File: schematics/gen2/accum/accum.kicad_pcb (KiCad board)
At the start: 2 copper layers, 100 x 101.6 mm, 14 parts, among them U1 74LS574, U2 74LS138, U3 74LS02, U4 74LS245, U5 74LS245, U6 74LS245

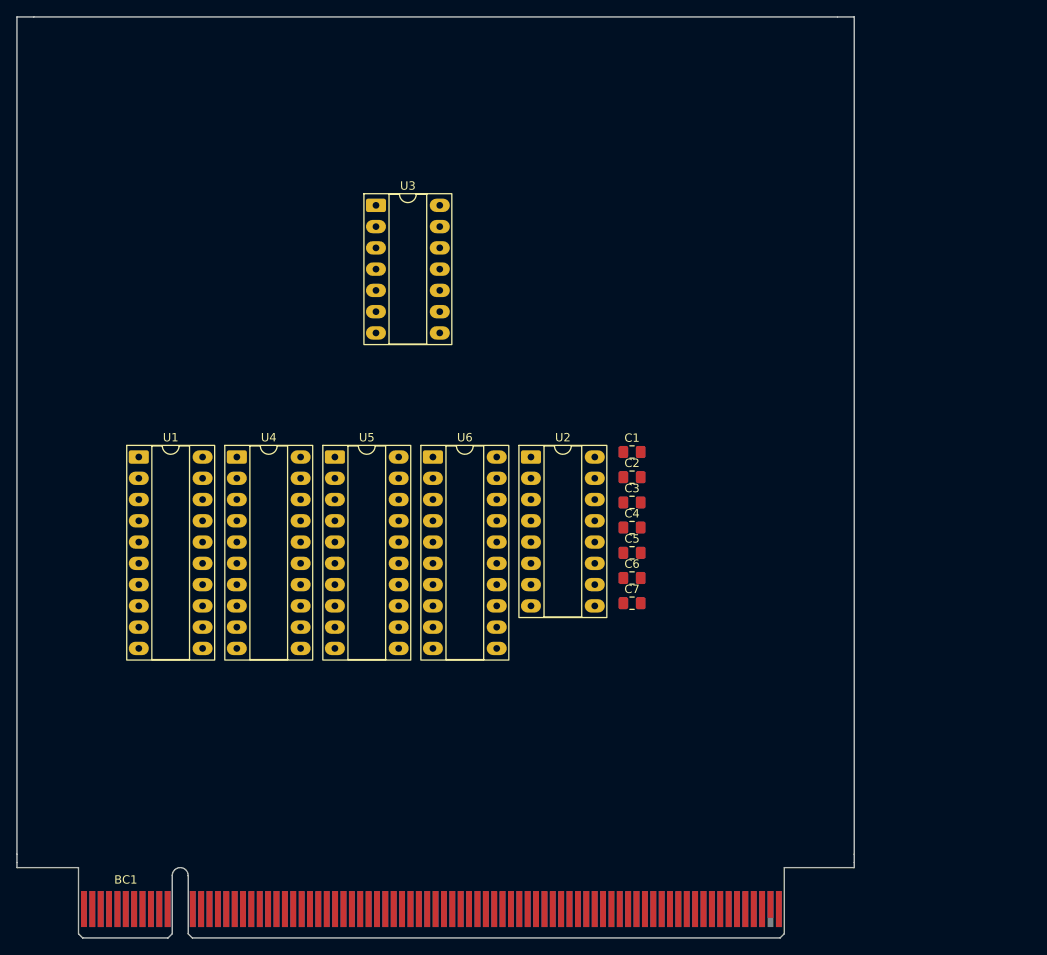
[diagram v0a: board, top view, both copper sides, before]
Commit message: fix: update accumulator schematic and routing rules
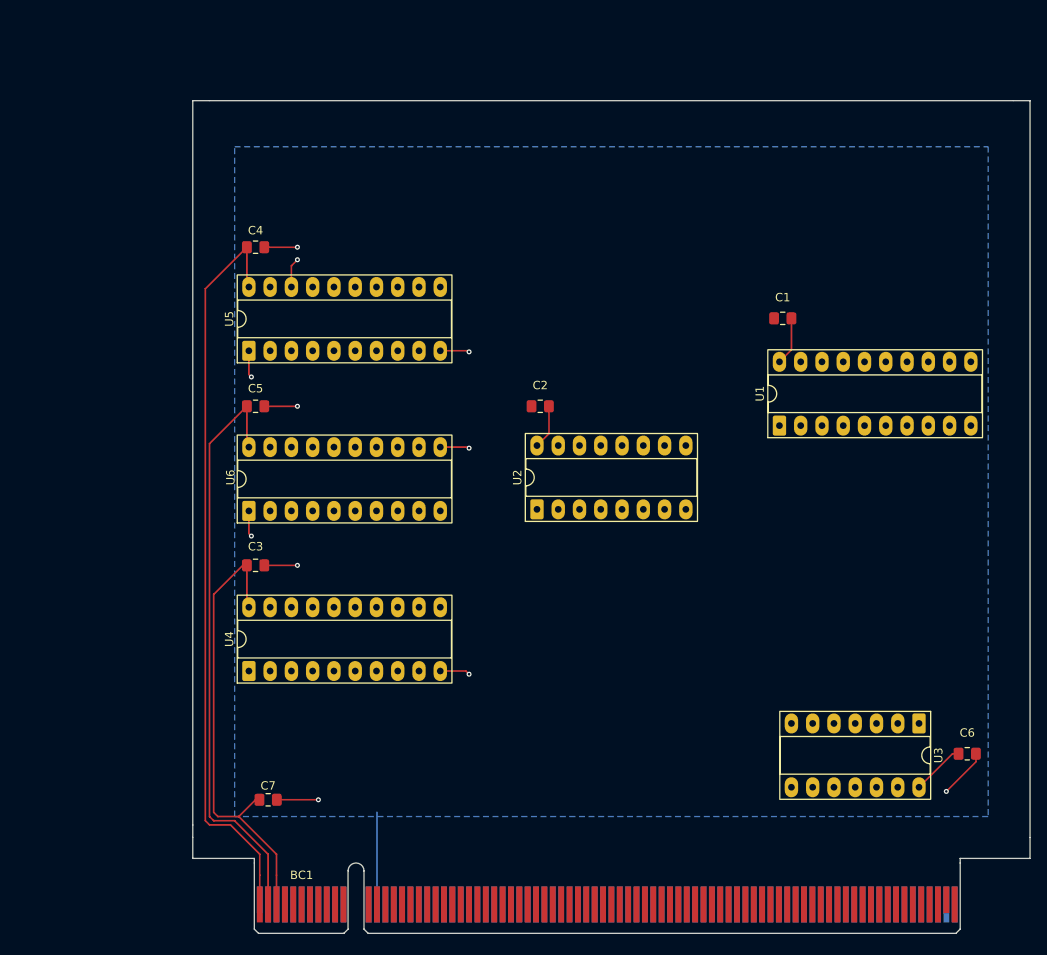
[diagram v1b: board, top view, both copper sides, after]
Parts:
- moved U3 89.6 mm to (186.7, 123.9), turned to -90 degrees
- moved U1 76.6 mm to (170.1, 88.3), turned to 90 degrees
- moved C4 56.1 mm to (107.5, 67.0)
- moved C7 49.4 mm to (109.0, 133.0)
- moved C5 48.2 mm to (107.5, 86.0)
- moved C3 45.6 mm to (107.5, 105.0)
- moved C6 45.2 mm to (192.5, 127.5)
- moved U4 25.6 mm to (106.7, 117.6), turned to 90 degrees
- moved C1 24.1 mm to (170.5, 75.5), turned to 180 degrees
- moved U6 22.9 mm to (106.7, 98.5), turned to 90 degrees
- moved BC1 21.0 mm to (108.0, 145.5)
- moved U5 16.3 mm to (106.7, 79.4), turned to 90 degrees
- moved C2 13.9 mm to (141.5, 86.0), turned to 180 degrees
- moved U2 6.29 mm to (141.1, 98.3), turned to 90 degrees
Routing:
- net VCC: track 0.00 -> 234.6 mm
- net GND: track 0.00 -> 54.3 mm, vias 0 -> 11
- added copper zone on B.Cu, net GND
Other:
- board size 100 x 101.6 mm -> 100 x 91.1 mm

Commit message: feat: accumulator pcb plate, with routes and gnd plate
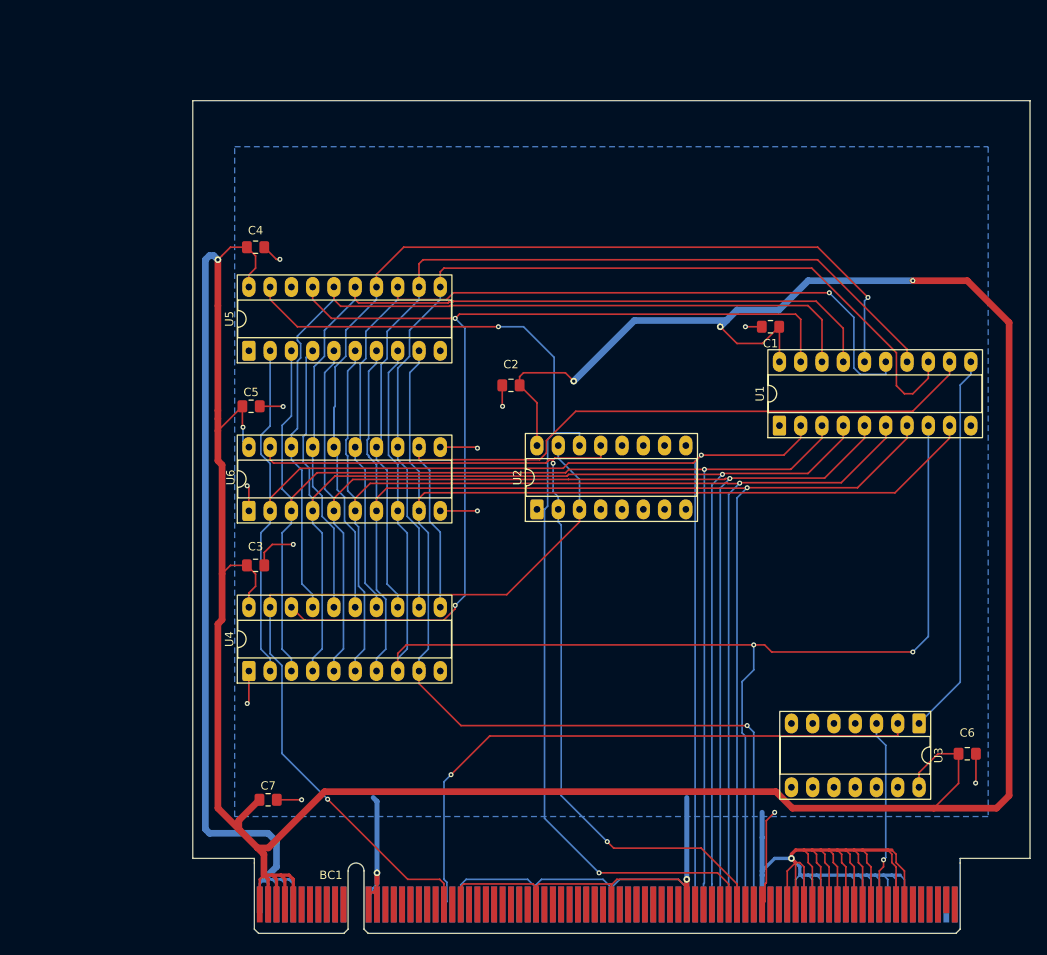
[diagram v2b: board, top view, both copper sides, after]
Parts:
- moved C2 4.30 mm to (138.0, 83.5)
- moved C1 1.77 mm to (169.0, 76.5)
- moved C5 0.54 mm to (107.0, 86.0)
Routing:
- net GND: track 54.3 -> 329.5 mm, vias 11 -> 15
- net VCC: track 234.6 -> 488.6 mm, vias 0 -> 5
- net /DATA7: track 0.00 -> 173.9 mm, vias 0 -> 1
- net /DATA6: track 0.00 -> 164.0 mm, vias 0 -> 2
- net /DATA0: track 0.00 -> 163.4 mm, vias 0 -> 1
- net /DATA1: track 0.00 -> 161.4 mm, vias 0 -> 1
- net /DATA2: track 0.00 -> 161.4 mm, vias 0 -> 1
- net /DATA3: track 0.00 -> 160.8 mm, vias 0 -> 1
- net /DATA4: track 0.00 -> 160.4 mm, vias 0 -> 1
- net /DATA5: track 0.00 -> 159.7 mm, vias 0 -> 1
- net /ACSHLEFT: track 0.00 -> 126.9 mm, vias 0 -> 2
- net /ACCUM0: track 0.00 -> 122.7 mm, vias 0 -> 2
- net /ACCUM3: track 0.00 -> 118.0 mm, vias 0 -> 1
- net /ACCUM6: track 0.00 -> 112.9 mm
- net /ACSHRIGHT: track 0.00 -> 111.5 mm, vias 0 -> 2
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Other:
- outline, holes or cut-outs redrawn

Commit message: fix: changed footprints in accum, added resistor and capacitor footrpint
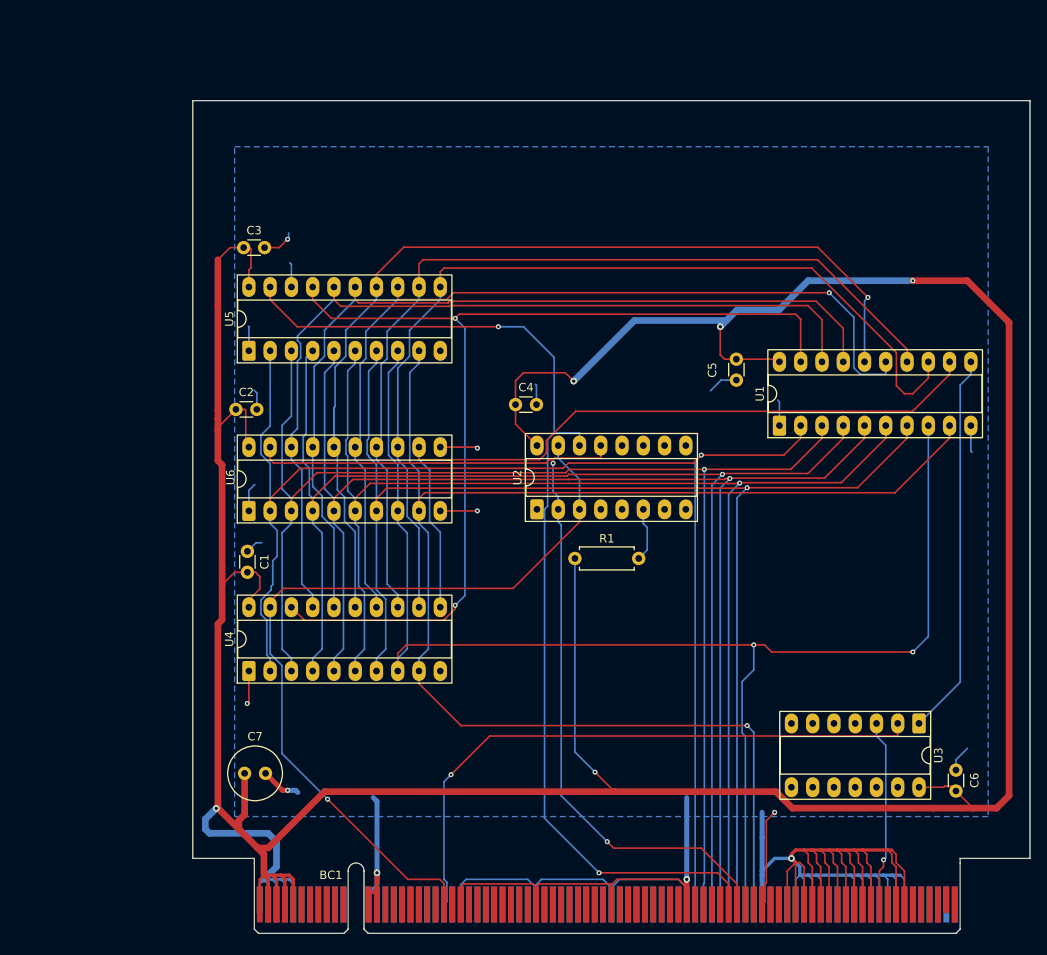
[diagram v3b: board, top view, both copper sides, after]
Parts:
- added R1: R, Resistor_THT:R_Axial_DIN0207_L6.3mm_D2.5mm_P7.62mm_Horizontal, F.Cu at (145.6, 104.2)
- C1, C2, C3, C4, C5, C6: footprint Capacitor_SMD:C_0805_2012Metric_Pad1.18x1.45mm_HandSolder -> Capacitor_THT:C_Disc_D3.0mm_W1.6mm_P2.50mm
- C7: footprint Capacitor_SMD:C_0805_2012Metric_Pad1.18x1.45mm_HandSolder -> Capacitor_THT:C_Radial_D6.3mm_H5.0mm_P2.50mm
- moved C1 69.0 mm to (106.5, 105.8), turned to 90 degrees
- moved C5 58.2 mm to (164.9, 80.4), turned to -90 degrees
- moved C3 38.0 mm to (106.1, 67.0)
- moved C4 36.3 mm to (138.6, 85.8)
- moved C2 33.0 mm to (105.2, 86.4), turned to 0 degrees
- moved C6 4.65 mm to (191.2, 131.9), turned to 90 degrees
- moved C7 4.23 mm to (106.2, 129.8)
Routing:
- net VCC: track 488.6 -> 444.7 mm
- net GND: track 329.5 -> 342.1 mm, vias 15 -> 9
- net Net-(U2-E3): track 0.00 -> 6.48 mm
- net /DATA0: track 163.4 -> 164.1 mm

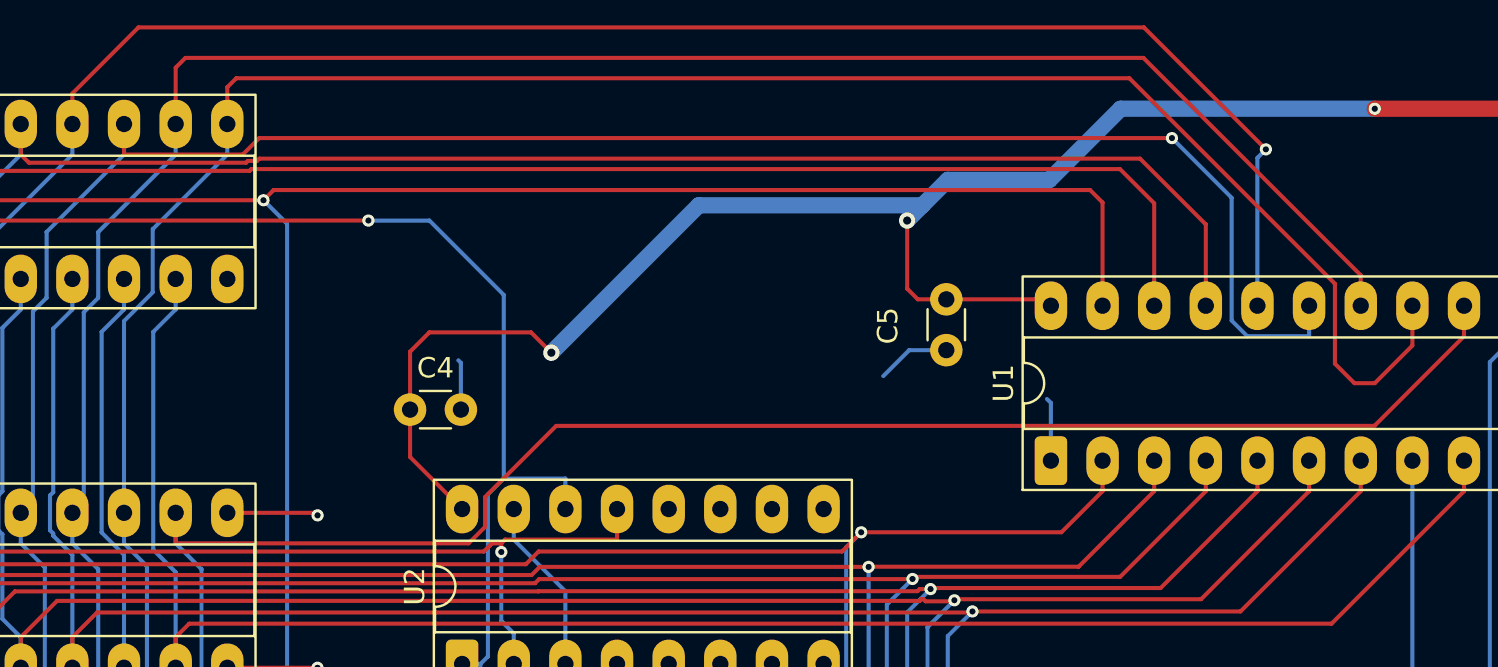
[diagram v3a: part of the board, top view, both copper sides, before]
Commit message: fix(accum): update segment connections and adjust routing
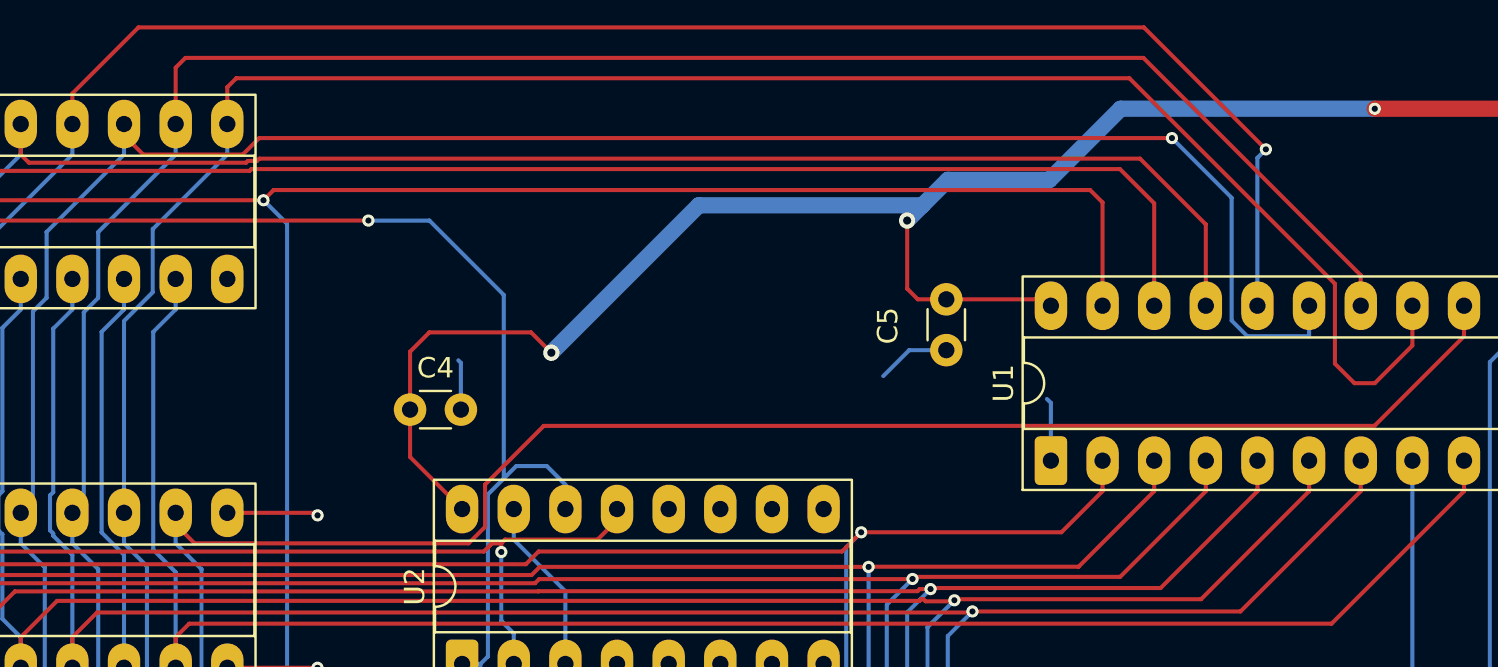
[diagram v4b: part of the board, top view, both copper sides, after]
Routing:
- net /ACSHRIGHT: track 111.5 -> 110.9 mm
- net /ACCUM4: track 110.6 -> 110.1 mm
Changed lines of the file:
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@@
+	)
+	(segment
+		(start 148.73 90.69)
+		(end 148.73 91.2367)
+		(width 0.2)
+		(layer "F.Cu")
+		(net 31)
 	)
 	(segment
@@
 	)
 	(segment
-		(start 148.73 90.69)
-		(end 148.73 92.1917)
-		(width 0.2)
-		(layer "F.Cu")
-		(net 31)
-	)
-	(segment
 		(start 142.4119 92.544)
 		(end 142.5782 92.3777)
@@
 	)
 	(segment
-		(start 148.73 92.1917)
+		(start 147.775 92.1917)
 		(end 143.223 92.1917)
 		(width 0.2)
@@
 		(start 150.2731 138.7731)
 		(end 160.7248 138.7731)
+		(width 0.2)
+		(layer "F.Cu")
+		(net 31)
+	)
+	(segment
+		(start 148.73 91.2367)
+		(end 147.775 92.1917)
 		(width 0.2)
 		(layer "F.Cu")
@@
 	)
 	(segment
+		(start 146.19 89.49)
+		(end 145.275 88.575)
+		(width 0.2)
+		(layer "B.Cu")
+		(net 94)
+	)
+	(segment
 		(start 143.1586 80.1586)
 		(end 143.1586 89.1883)
@@
 	)
 	(segment
+		(start 146.19 90.69)
+		(end 146.19 89.49)
+		(width 0.2)
+		(layer "B.Cu")
+		(net 94)
+	)
+	(segment
 		(start 142.01 135.2055)
 		(end 142.01 98.31)
@@
 	)
 	(segment
-		(start 146.19 89.1883)
-		(end 143.1586 89.1883)
+		(start 145.275 88.575)
+		(end 143.7719 88.575)
 		(width 0.2)
 		(layer "B.Cu")
@@
 	)
 	(segment
-		(start 146.19 90.69)
-		(end 146.19 89.1883)
+		(start 143.7719 88.575)
+		(end 143.1586 89.1883)
 		(width 0.2)
 		(layer "B.Cu")
@@
 	)
 	(segment
+		(start 127.02 91.4477)
+		(end 127.95 92.3777)
+		(width 0.2)
+		(layer "F.Cu")
+		(net 100)
+	)
+	(segment
+		(start 185.9816 86.6001)
+		(end 145.1249 86.6001)
+		(width 0.2)
+		(layer "F.Cu")
+		(net 100)
+	)
+	(segment
+		(start 190.39 80.69)
+		(end 190.39 82.1917)
+		(width 0.2)
+		(layer "F.Cu")
+		(net 100)
+	)
+	(segment
+		(start 145.1249 86.6001)
+		(end 142.2385 89.4865)
+		(width 0.2)
+		(layer "F.Cu")
+		(net 100)
+	)
+	(segment
 		(start 142.2385 91.5691)
 		(end 141.4299 92.3777)
@@
 	)
 	(segment
-		(start 190.39 80.69)
-		(end 190.39 82.1917)
+		(start 190.39 82.1917)
+		(end 185.9816 86.6001)
 		(width 0.2)
 		(layer "F.Cu")
@@
 	)
 	(segment
-		(start 185.9816 86.6001)
-		(end 145.7374 86.6001)
+		(start 141.4299 92.3777)
+		(end 127.95 92.3777)
 		(width 0.2)
 		(layer "F.Cu")
@@
 	)
 	(segment
-		(start 145.7374 86.6001)
-		(end 142.2385 90.099)
-		(width 0.2)
-		(layer "F.Cu")
+		(start 127.02 90.876)
+		(end 127.02 91.4477)
+		(width 0.2)
+		(layer "F.Cu")
+		(net 100)
+	)
+	(segment
+		(start 142.2385 89.4865)
+		(end 142.2385 91.5691)
+		(width 0.2)
+		(layer "F.Cu")
+		(net 100)
+	)
+	(segment
+		(start 128.29 93.6477)
+		(end 128.29 99.7549)
+		(width 0.2)
+		(layer "B.Cu")
 		(net 100)
 	)
@@
 		(end 127.02 92.3777)
 		(width 0.2)
-		(layer "F.Cu")
-		(net 100)
-	)
-	(segment
-		(start 190.39 82.1917)
-		(end 185.9816 86.6001)
-		(width 0.2)
-		(layer "F.Cu")
-		(net 100)
-	)
-	(segment
-		(start 142.2385 90.099)
-		(end 142.2385 91.5691)
-		(width 0.2)
-		(layer "F.Cu")
-		(net 100)
-	)
-	(segment
-		(start 141.4299 92.3777)
-		(end 127.02 92.3777)
-		(width 0.2)
-		(layer "F.Cu")
-		(net 100)
-	)
-	(segment
-		(start 128.29 93.6477)
-		(end 128.29 99.7549)
-		(width 0.2)
-		(layer "B.Cu")
-		(net 100)
-	)
-	(segment
-		(start 127.02 90.876)
-		(end 127.02 92.3777)
-		(width 0.2)
 		(layer "B.Cu")
 		(net 100)
@@
 	(segment
 		(start 124.48 71.752)
-		(end 124.48 73.2537)
+		(end 124.48 72.3087)
+		(width 0.2)
+		(layer "F.Cu")
+		(net 101)
+	)
+	(segment
+		(start 124.48 72.3087)
+		(end 125.425 73.2537)
 		(width 0.2)
 		(layer "F.Cu")
@@
 	(segment
 		(start 130.3195 73.2537)
-		(end 124.48 73.2537)
-		(width 0.2)
-		(layer "F.Cu")
+		(end 125.425 73.2537)
+		(width 0.2)
+		(layer "F.Cu")
